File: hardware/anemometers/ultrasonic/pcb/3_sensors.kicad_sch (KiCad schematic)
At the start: 17 parts, among them U10 APDS-9250, U11 AS3935, U8 BME280, U9 BMX160

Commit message: DRC clear
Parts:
- removed ?: A_A4, ProDoc_Qin-easyedapro:, symbol ProDoc_Qin-easyedapro:A_A4
- renumbered ANT to ANT1
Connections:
- no-connect marks 0 -> 7

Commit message: update
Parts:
- removed ANT1: INDUCTORMA5532, ProDoc_Qin-easyedapro:INDUCTOR_COILCRAFT_MA5532-AE, symbol ProDoc_Qin-easyedapro:INDUCTORMA5532
- removed C53: 100nF, ProDoc_Qin-easyedapro:C0402, symbol ProDoc_Qin-easyedapro:100nF
- removed C54: 1uF, ProDoc_Qin-easyedapro:C0402, symbol ProDoc_Qin-easyedapro:1uF
- removed C55: 10uF, ProDoc_Qin-easyedapro:C0603, symbol ProDoc_Qin-easyedapro:10uF
- removed C56: 1nF, ProDoc_Qin-easyedapro:C0402, symbol ProDoc_Qin-easyedapro:1nF
- removed R42: 10K, ProDoc_Qin-easyedapro:R0402, symbol ProDoc_Qin-easyedapro:10K
- removed U10: APDS-9250, ProDoc_Qin-easyedapro:ADPS-9250, symbol ProDoc_Qin-easyedapro:APDS-9250
- removed U11: AS3935, ProDoc_Qin-easyedapro:16LDMLPQ, symbol ProDoc_Qin-easyedapro:AS3935
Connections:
- no-connect marks 7 -> 4
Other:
- note removed: "AM3935 has internal 10k pull up on SCL"
- moved on the sheet: C47, C50, C51, C52, R40, R41, U8, U9

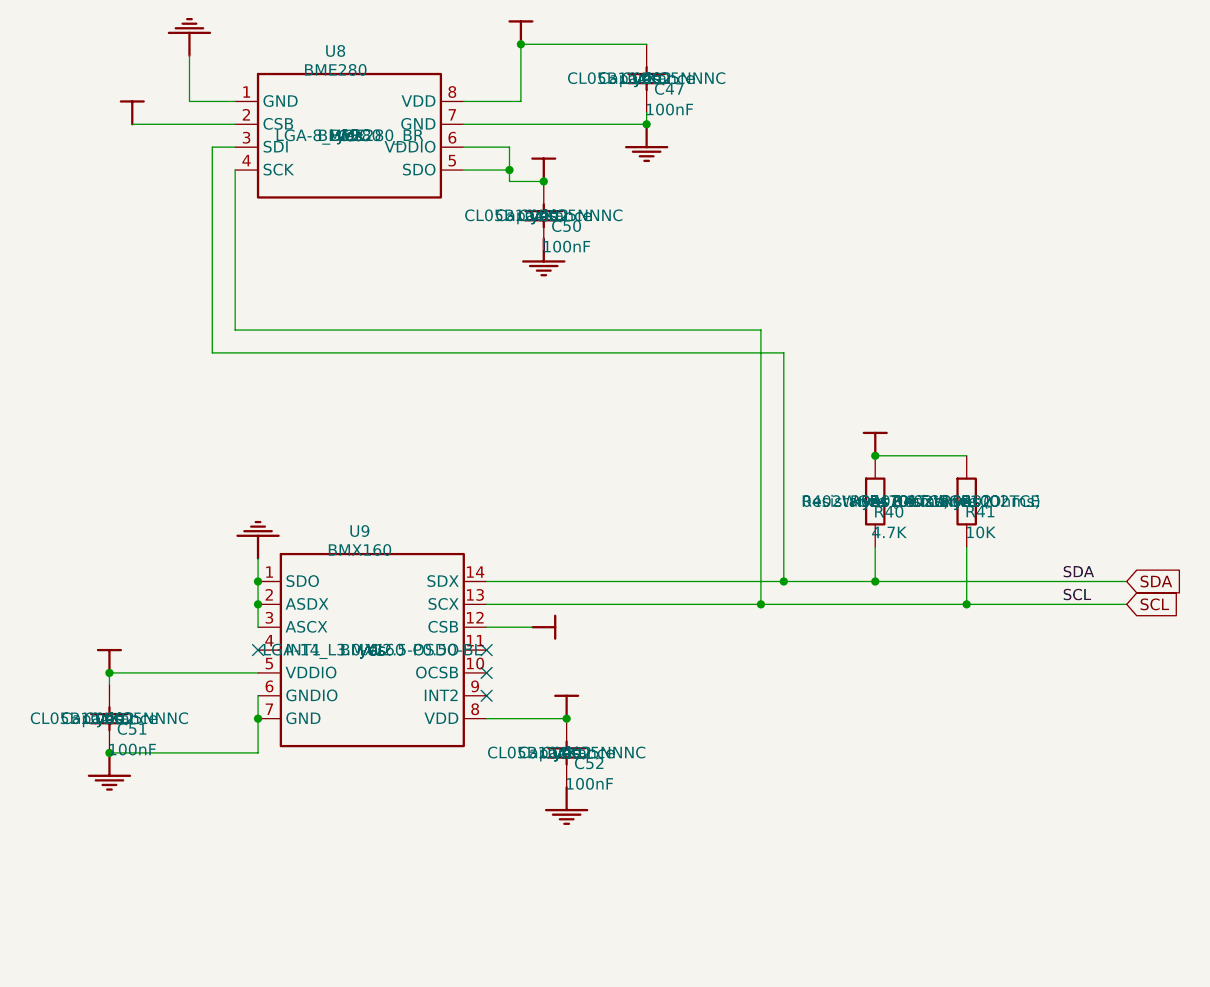
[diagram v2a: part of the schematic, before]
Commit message: Update to BMI270
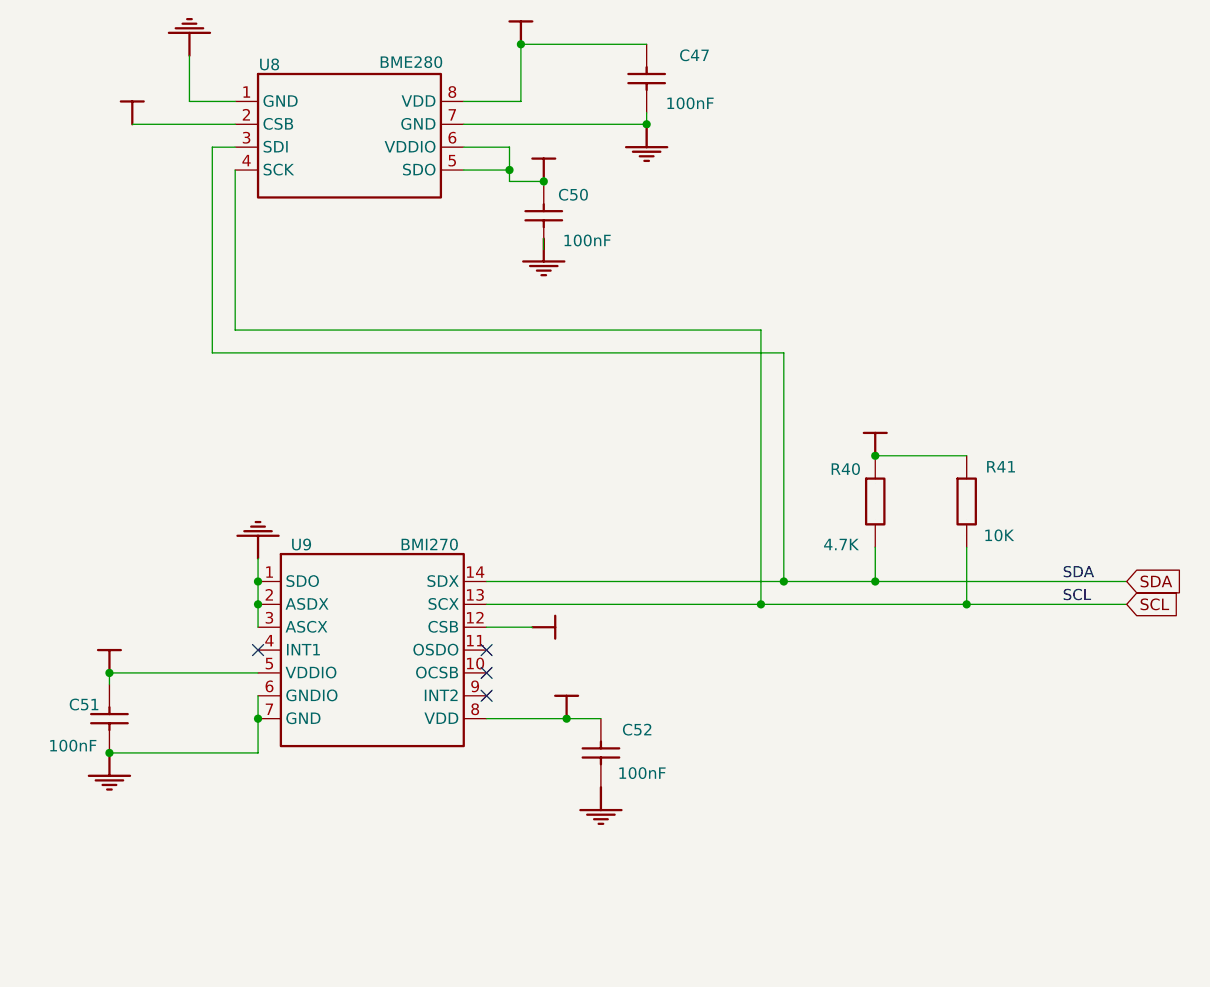
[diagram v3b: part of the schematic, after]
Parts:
- U9: value BMX160 -> BMI270; Manufacturer Part BMI160 -> BMI270; Supplier Digi-Key -> LCSC; Supplier Part 828-1087-1-ND -> C2836813
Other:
- moved on the sheet: C52

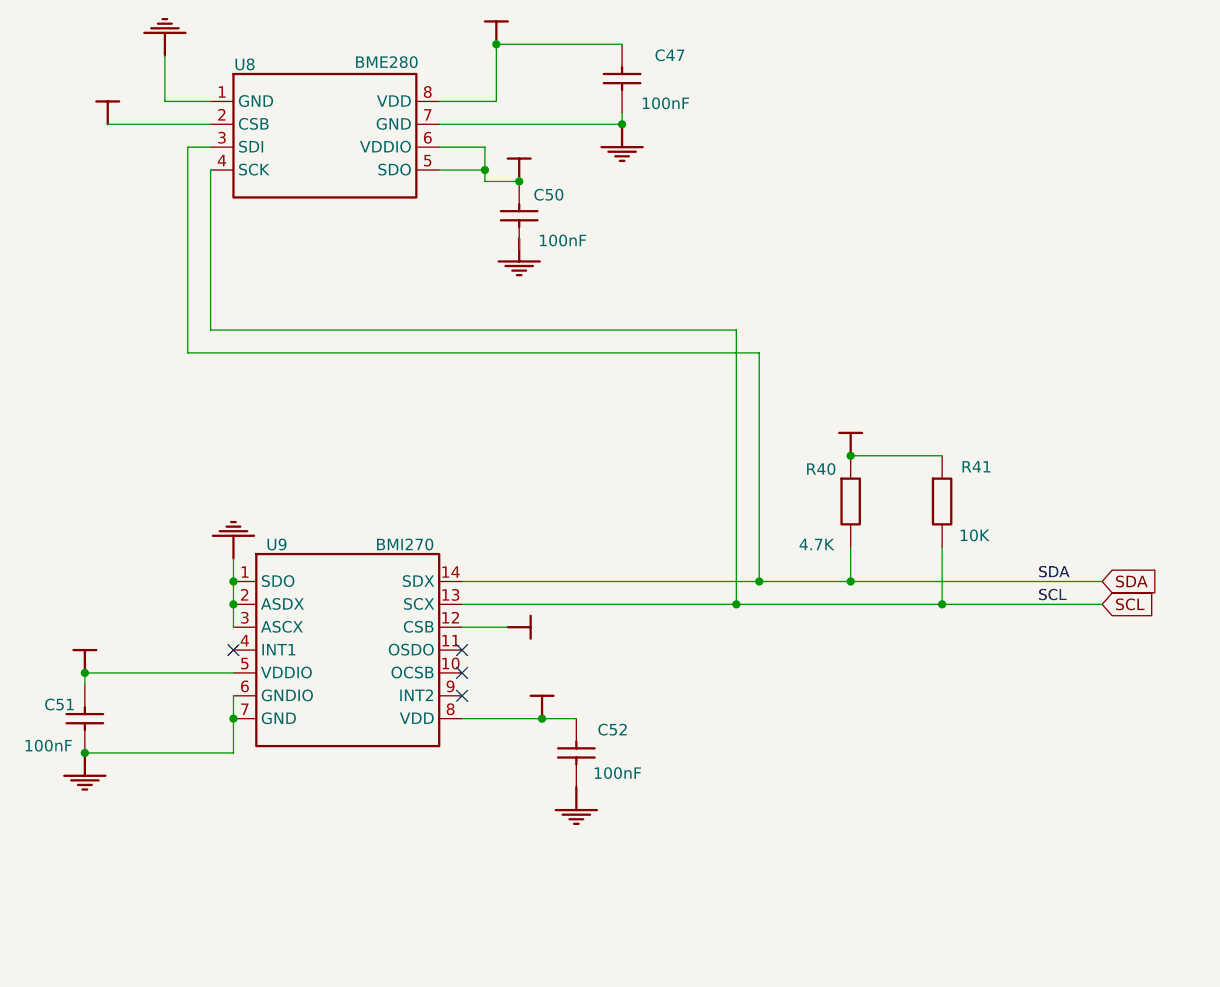
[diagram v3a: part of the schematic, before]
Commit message: Remove BME280
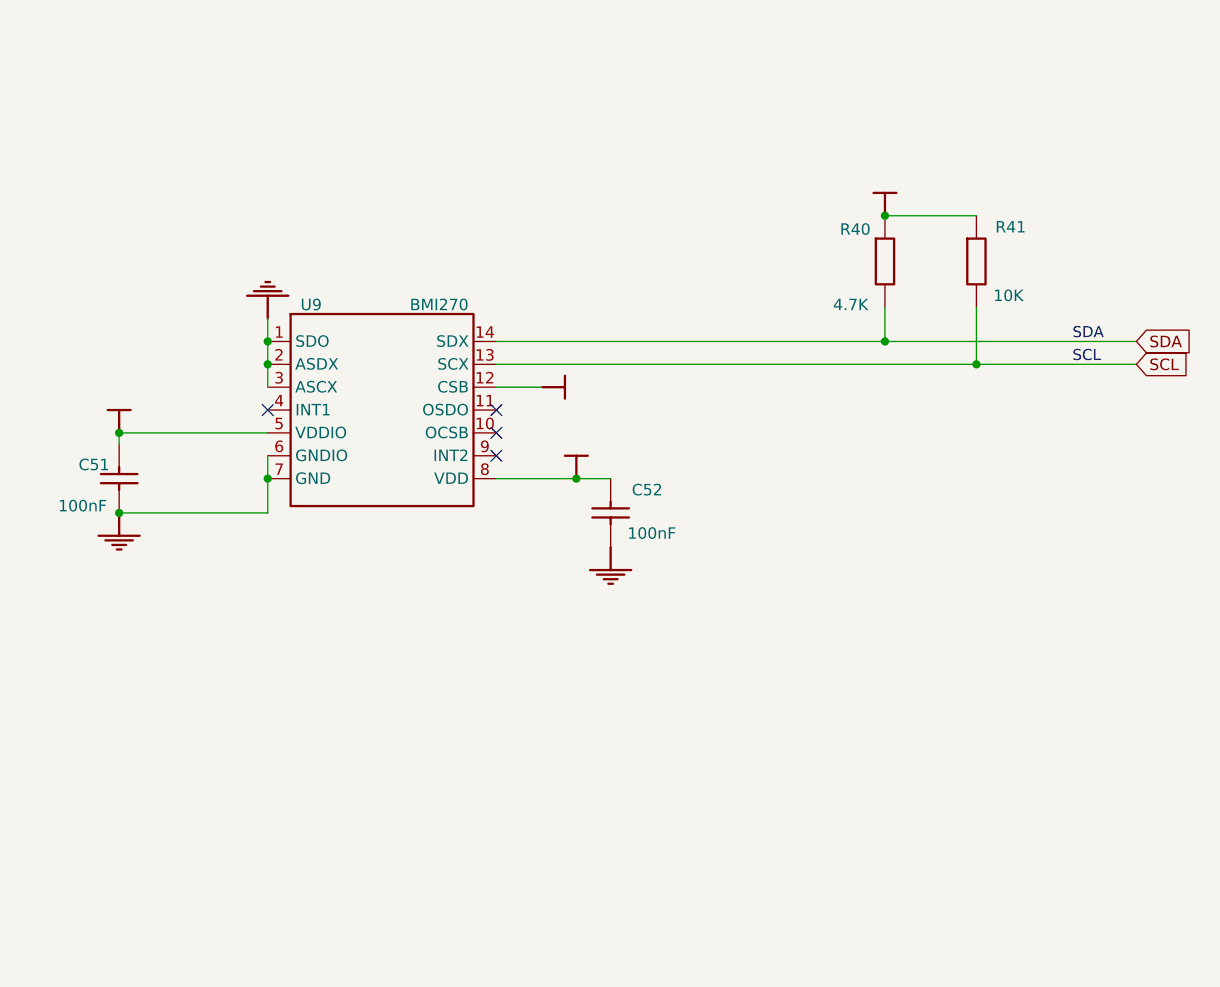
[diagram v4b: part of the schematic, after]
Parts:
- removed C47, C50: 100nF, ProDoc_Qin-easyedapro:C0402, symbol ProDoc_Qin-easyedapro:100nF
- removed U8: BME280, ProDoc_Qin-easyedapro:LGA-8_BME280_BR, symbol ProDoc_Qin-easyedapro:BME280
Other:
- moved on the sheet: C51, C52, R40, R41, U9
